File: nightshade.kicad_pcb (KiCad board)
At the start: 4 copper layers, 187.3 x 76.2 mm, 101 parts, among them J1 Bus_ISA_16bit, J2 DE15_Plug_HighDensity_Mountin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, J3 Conn_02x13_Odd_Even, Q1 MMBT3904, U1 GD542x_ISA, U10 74HCT244, U11 SOJ_256Kx16, U12 SOJ_256Kx16, U2 SOJ_256Kx16, U3 SOJ_256Kx16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

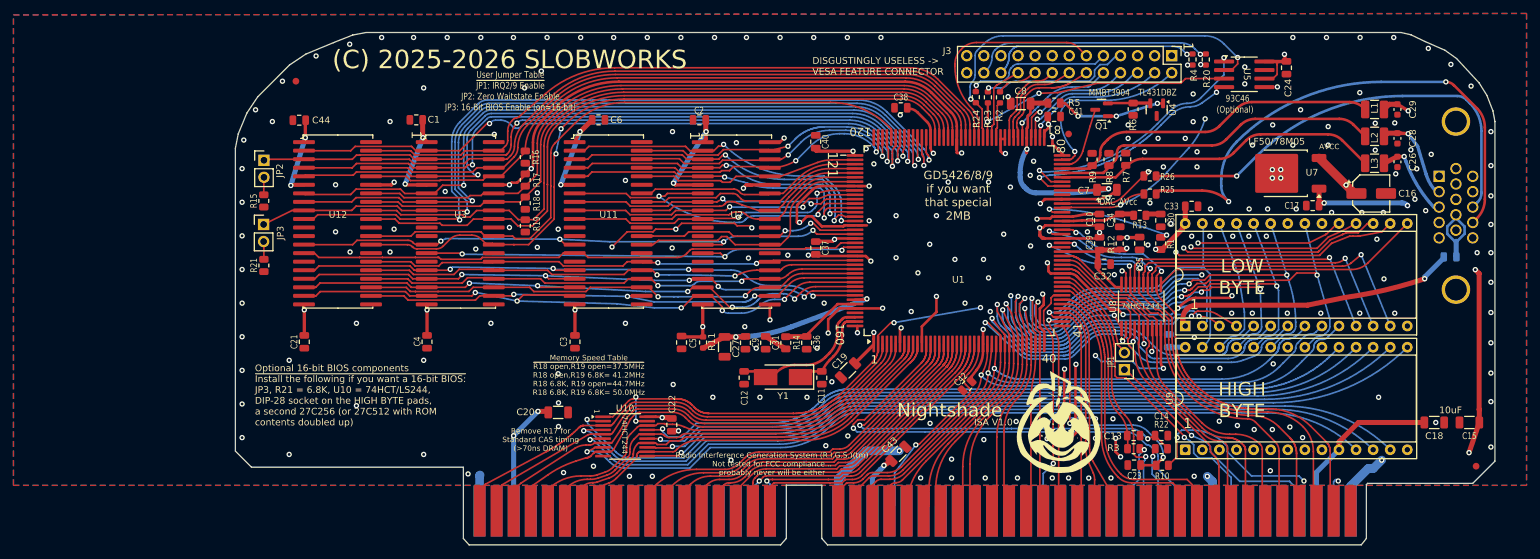
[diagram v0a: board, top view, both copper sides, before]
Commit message: Add files via upload
1.0a - Moderate clean-up of routing in some areas, improving ground pour contiguity and redistributing some of the ground pour vias so they're a little smarter placed in general.
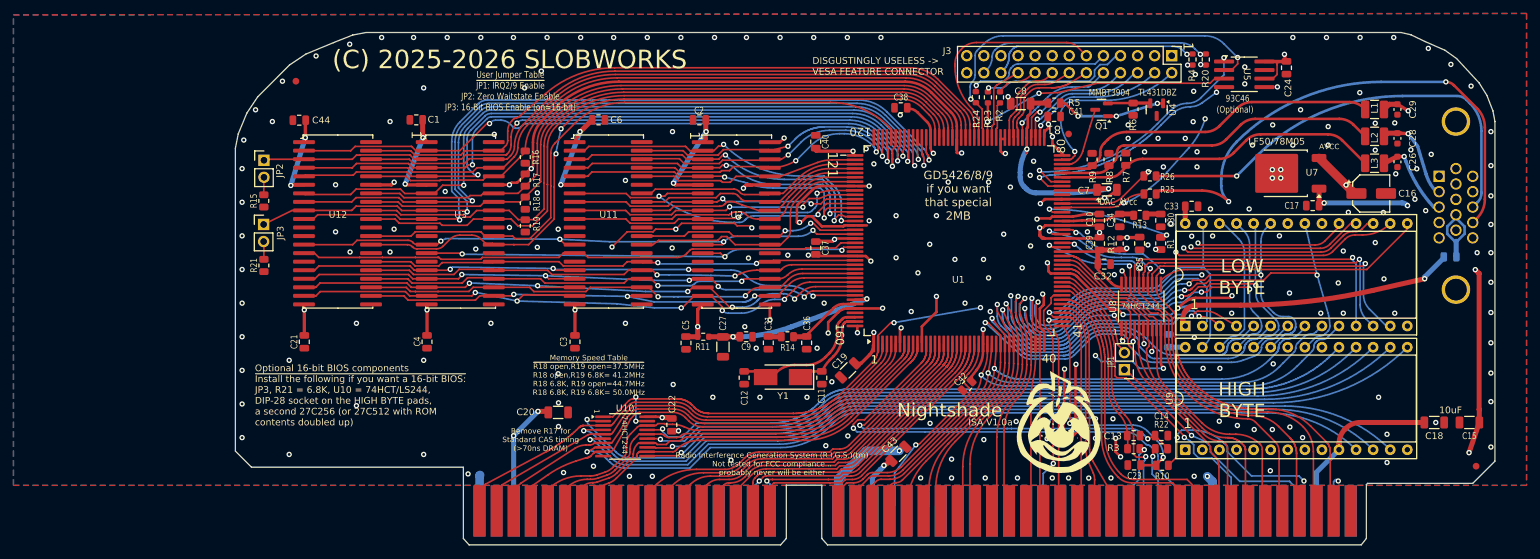
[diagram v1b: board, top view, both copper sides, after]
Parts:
- moved R14 0.93 mm to (129.1, 127.0), turned to 180 degrees
- moved C9 0.91 mm to (123.0, 127.0), turned to 180 degrees
- moved R11 0.85 mm to (116.6, 127.0), turned to 180 degrees
- moved C5 0.66 mm to (114.0, 127.9)
- moved C31 0.40 mm to (126.2, 127.9)
- moved C27 0.25 mm to (119.5, 128.5)
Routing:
- net GND: track 344.8 -> 333.6 mm, vias 254 -> 252
- net /+5V: track 350.5 -> 344.5 mm
- net /D0: track 43.6 -> 46.5 mm
- net /SA9: track 99.8 -> 97.4 mm
- net /D1: track 44.2 -> 46.1 mm
- net Net-(C31-Pad1): track 3.53 -> 1.95 mm
- net /MCLKVCC: track 29.1 -> 27.7 mm
- net /MFILTER: track 12.4 -> 11.2 mm
- net /SA13: track 85.2 -> 86.4 mm
- net /SA8: track 99.8 -> 98.8 mm
- net /SA11: track 97.7 -> 96.8 mm
- net /D3: track 40.6 -> 41.4 mm
- net /D7: track 43.4 -> 44.1 mm
- net /VSYNC: track 40.0 -> 39.5 mm
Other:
- board text added: "ISA V1.0a"
- board text removed: "ISA V1.0"

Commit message: Add files via upload
Cheaper parts that do not affect function! Yay!
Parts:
- C1, C10, C17, C2, C21, C22, C24, C25, C3, C32, C33, C34, C35, C36, C37, C38, C39, C4, C40, C42, C44, C5, C6, C9: value 0.22u -> 0.1u
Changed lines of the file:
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@@
 			)
 		)
-		(property "Value" "0.22u"
+		(property "Value" "0.1u"
 			(at -0.01 -2.35 0)
 			(layer "F.Fab")
@@
 			)
 		)
-		(property "Value" "0.22u"
+		(property "Value" "0.1u"
 			(at -1.525 1.425 90)
 			(layer "F.Fab")
@@
 			)
 		)
-		(property "Value" "0.22u"
+		(property "Value" "0.1u"
 			(at 0.225 -1.2 0)
 			(layer "F.Fab")
@@
 			)
 		)
-		(property "Value" "0.22u"
+		(property "Value" "0.1u"
 			(at 4.325 -0.05 90)
 			(layer "F.Fab")
@@
 			)
 		)
-		(property "Value" "0.22u"
+		(property "Value" "0.1u"
 			(at 0.125 -2.355 90)
 			(layer "F.Fab")
@@
 			)
 		)
-		(property "Value" "0.22u"
+		(property "Value" "0.1u"
 			(at 0 1.68 90)
 			(layer "F.Fab")
@@
 			)
 		)
-		(property "Value" "0.22u"
+		(property "Value" "0.1u"
 			(at -2.575 0.925 0)
 			(layer "F.Fab")
@@
 			)
 		)
-		(property "Value" "0.22u"
+		(property "Value" "0.1u"
 			(at -2.38 0.7 90)
 			(layer "F.Fab")
@@
 			)
 		)
-		(property "Value" "0.22u"
+		(property "Value" "0.1u"
 			(at -1.775 -1.525 90)
 			(layer "F.Fab")
@@
 			)
 		)
-		(property "Value" "0.22u"
+		(property "Value" "0.1u"
 			(at -2.675 -0.55 45)
 			(layer "F.Fab")
@@
 			)
 		)
-		(property "Value" "0.22u"
+		(property "Value" "0.1u"
 			(at 1.35 -1.45 0)
 			(layer "F.Fab")
@@
 			)
 		)
-		(property "Value" "0.22u"
+		(property "Value" "0.1u"
 			(at -2.575 1.65 0)
 			(layer "F.Fab")
@@
 			)
 		)
-		(property "Value" "0.22u"
+		(property "Value" "0.1u"
 			(at 2.55 1.1 90)
 			(layer "F.Fab")
@@
 			)
 		)
-		(property "Value" "0.22u"
+		(property "Value" "0.1u"
 			(at -3.675 -0.025 90)
 			(layer "F.Fab")
@@
 			)
 		)
-		(property "Value" "0.22u"
+		(property "Value" "0.1u"
 			(at -2.45 0.875 0)
 			(layer "F.Fab")
@@
 			)
 		)
-		(property "Value" "0.22u"
+		(property "Value" "0.1u"
 			(at 0 1.68 90)
 			(layer "F.Fab")
@@
 			)
 		)
-		(property "Value" "0.22u"
+		(property "Value" "0.1u"
 			(at 0 1.68 90)
 			(layer "F.Fab")
@@
 			)
 		)
-		(property "Value" "0.22u"
+		(property "Value" "0.1u"
 			(at 0 1.68 90)
 			(layer "F.Fab")
@@
 			)
 		)
-		(property "Value" "0.22u"
+		(property "Value" "0.1u"
 			(at 0 1.68 90)
 			(layer "F.Fab")
@@
 			)
 		)
-		(property "Value" "0.22u"
+		(property "Value" "0.1u"
 			(at 0 1.68 0)
 			(layer "F.Fab")
@@
 			)
 		)
-		(property "Value" "0.22u"
+		(property "Value" "0.1u"
 			(at 0 1.68 90)
 			(layer "F.Fab")
@@
 			)
 		)
-		(property "Value" "0.22u"
+		(property "Value" "0.1u"
 			(at 0 1.68 0)
 			(layer "F.Fab")
@@
 			)
 		)
-		(property "Value" "0.22u"
+		(property "Value" "0.1u"
 			(at 0 1.68 0)
 			(layer "F.Fab")
@@
 			)
 		)
-		(property "Value" "0.22u"
+		(property "Value" "0.1u"
 			(at 0 -1.68 90)
 			(layer "B.Fab")

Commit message: Add files via upload
Replaced all textual references to 'Killer Tomato' to less copyright infringing alternatives. Graphics are not changed yet, they will be eventually once time permits.
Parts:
- removed the G*** at (97.6, 117.8)
- removed the G*** at (98.5, 102.0)
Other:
- board text added: "GIVE ME THE TWO MEGABYTES!"
- board text added: "I'm very hungry!"
- board text added: "WHAT'RE YOU LOOKING AT OVER HERE?"
- board text removed: "HELP!"
- board text removed: "What happens when you take"
- board text removed: "You get a..."
- board text removed: "a rat bite me BITE IT BACK"
- board text removed: "and jack it all up?"
- board text removed: "ddcc48611957699eb0f441b2b0da33a4"
- board text removed: "or, {dblquote}What Happens When You Take A Joke To Its Logical Conclusion{dblquote}"
